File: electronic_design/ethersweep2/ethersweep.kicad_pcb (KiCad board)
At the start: 2 copper layers, 79 x 38 mm, 69 parts, among them J1 AVR-ISP-6, J2 Conn_01x02_Male, J3 Conn_01x04_Female, J4 Conn_01x02_Male, J5 Conn_01x02_Male, J6 HR911105A, J7 Conn_01x06_Female, J8 AVR-ISP-6, J9 Conn_01x06_Male, M1 Stepper_Motor_bipolar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

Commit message: small routing changes
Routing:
- net MISO: track 34.5 -> 36.3 mm
- net GND: vias 177 -> 192
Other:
- outline, holes or cut-outs redrawn

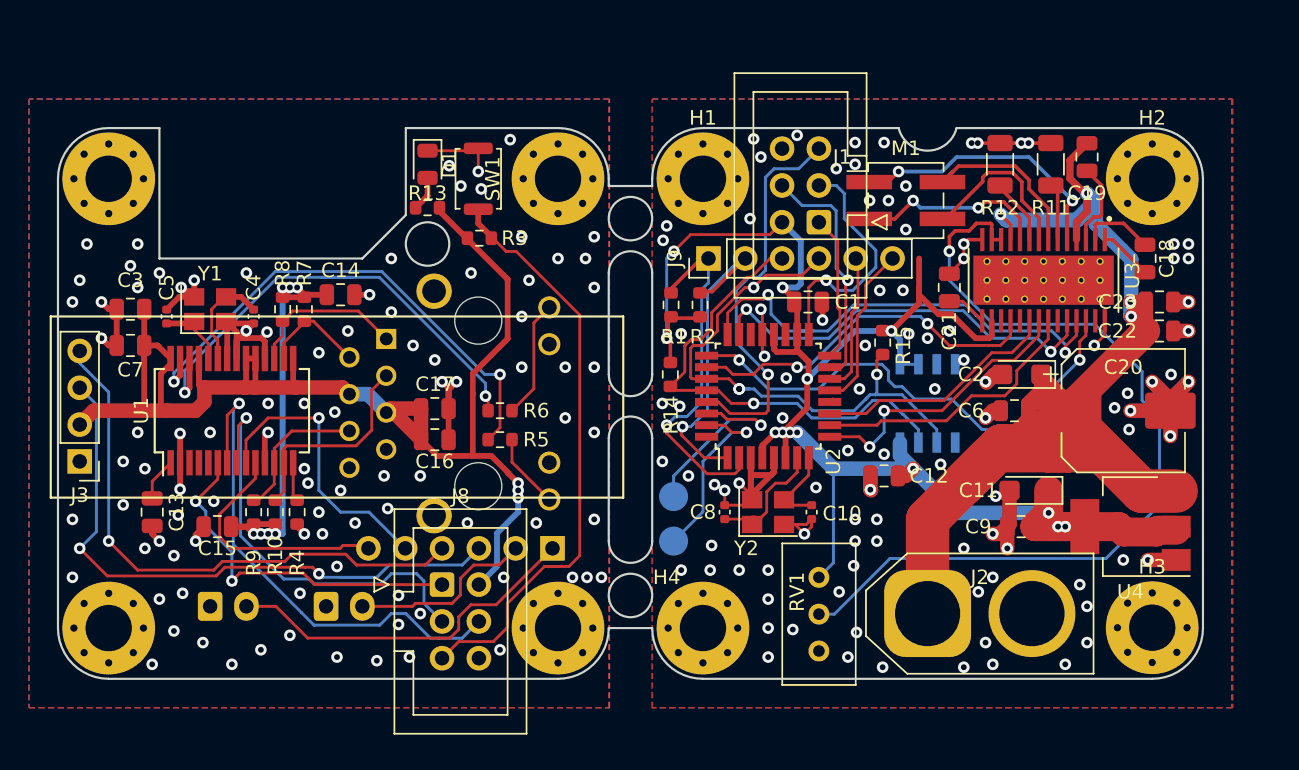
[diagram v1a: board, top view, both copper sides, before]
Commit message: added LCSC part numbers and changed some components for cheap manufacturing
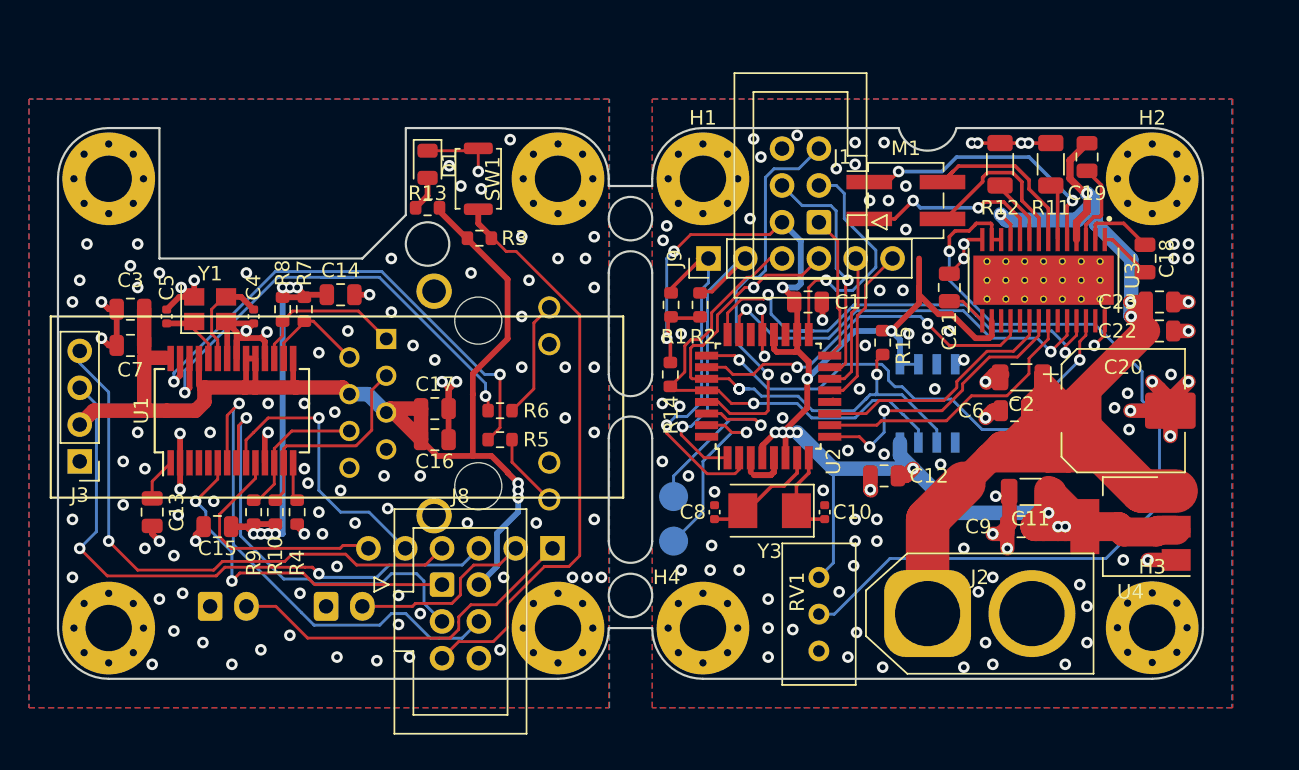
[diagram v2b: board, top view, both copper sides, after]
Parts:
- removed Y2: Crystal_8MHz, Crystal:Crystal_SMD_3225-4Pin_3.2x2.5mm
- added Y3: Crystal, Crystal:Crystal_SMD_5032-2Pin_5.0x3.2mm, F.Cu at (171.6, 107.4)
- C11, C2: value C22uF -> C4.7uF; footprint Capacitor_Tantalum_SMD:CP_EIA-3216-12_Kemet-S -> Capacitor_SMD:C_1206_3216Metric
- moved C10 0.90 mm to (175.4, 107.5), turned to 270 degrees
- moved C8 0.70 mm to (167.8, 107.5)
- moved C2 0.20 mm to (189.0, 98.2)
- moved C11 0.14 mm to (189.6, 106.1)
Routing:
- net GND: track 114.0 -> 92.9 mm, vias 192 -> 188
- net +3V3: track 226.6 -> 224.7 mm
- net +12V: track 116.7 -> 117.8 mm
- net Net-(C10-Pad2): track 5.66 -> 6.49 mm

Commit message: footprint changes, LCSC parts assigned, design changes
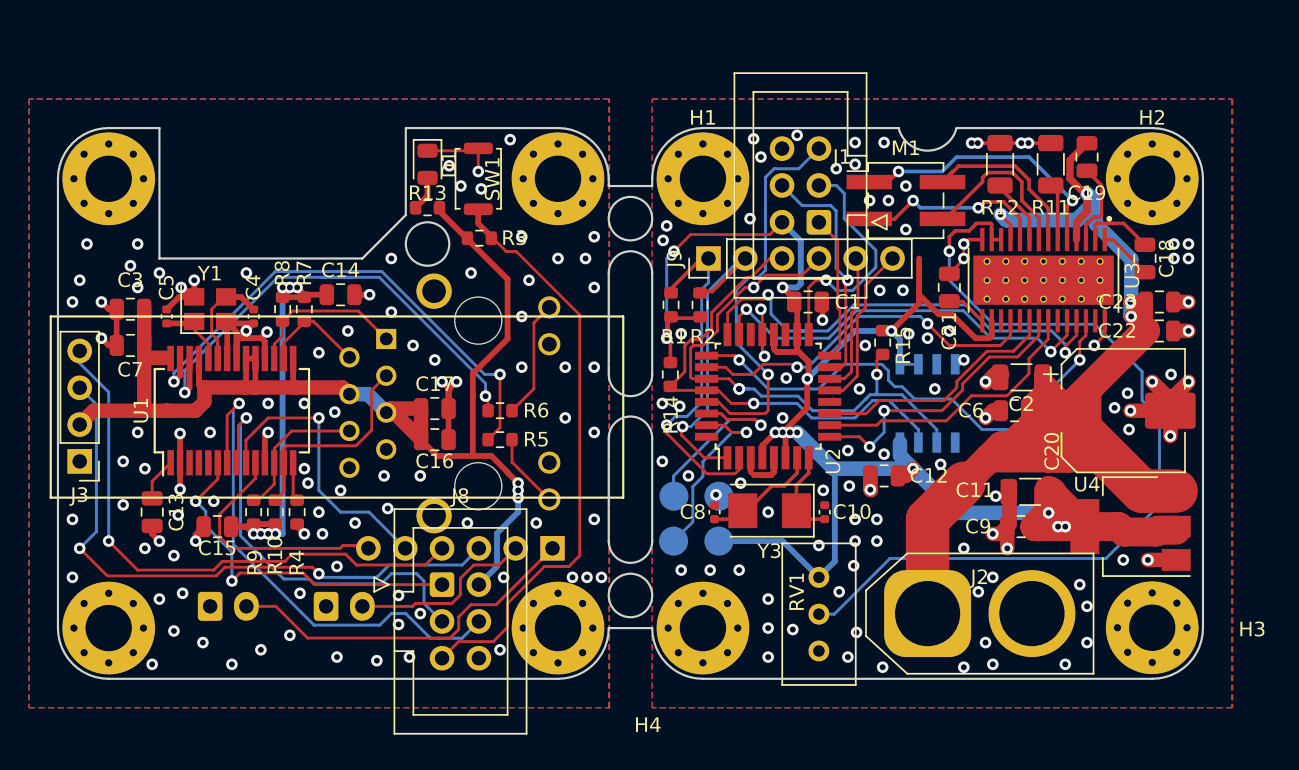
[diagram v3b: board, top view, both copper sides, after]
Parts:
- added TP1: TestPoint, TestPoint:TestPoint_Pad_D2.0mm, B.Cu at (168.1, 109.5)
- added TP2: TestPoint, TestPoint:TestPoint_Pad_D2.0mm, B.Cu at (168.1, 106.4)
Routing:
- net +3V3: track 224.7 -> 232.7 mm
- net GND: vias 188 -> 191
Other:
- board text added: "3.3V>"
- board text added: "GND>"
- board text added: "ethersweep"
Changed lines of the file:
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@@
   (general
     (thickness 1.6)
-    (drawings 47)
-    (tracks 1198)
+    (drawings 52)
+    (tracks 1206)
     (zones 0)
-    (modules 69)
+    (modules 71)
     (nets 62)
   )
@@
     (0 F.Cu signal)
     (31 B.Cu signal)
-    (32 B.Adhes user)
-    (33 F.Adhes user)
+    (32 B.Adhes user hide)
+    (33 F.Adhes user hide)
     (34 B.Paste user)
     (35 F.Paste user)
@@
   )
   (setup
-    (last_trace_width 2)
+    (last_trace_width 0.4)
     (user_trace_width 0.2)
     (user_trace_width 0.4)
@@
     (tags "mounting hole 3.2mm m3")
     (attr virtual)
-    (fp_text reference H4 (at -2.5 -3.5) (layer F.SilkS)
+    (fp_text reference H4 (at -3.8 6.7) (layer F.SilkS)
       (effects (font (size 1 1) (thickness 0.15)))
     )
@@
     (tags "mounting hole 3.2mm m3")
     (attr virtual)
-    (fp_text reference H3 (at 0 -4.2) (layer F.SilkS)
+    (fp_text reference H3 (at 6.9 0.124999) (layer F.SilkS)
       (effects (font (size 1 1) (thickness 0.15)))
     )
@@
     (tags "capacitor electrolytic")
     (attr smd)
-    (fp_text reference C20 (at 0 -3) (layer F.SilkS)
+    (fp_text reference C20 (at -4.9 2.8 90) (layer F.SilkS)
       (effects (font (size 1 1) (thickness 0.15)))
     )
@@
     (tags resistor)
     (attr smd)
-    (fp_text reference R9 (at -3.5 0 -90) (layer F.SilkS)
+    (fp_text reference R9 (at -3.5 0.1 90) (layer F.SilkS)
       (effects (font (size 1 1) (thickness 0.15)))
     )
@@
     (tags "CMS SOT")
     (attr smd)
-    (fp_text reference U4 (at 0 -4.5) (layer F.SilkS)
+    (fp_text reference U4 (at 3 2.9) (layer F.SilkS)
       (effects (font (size 1 1) (thickness 0.15)))
     )
@@
     (tags "mounting hole 3.2mm m3")
     (attr virtual)
-    (fp_text reference H7 (at 0 4.2) (layer B.SilkS)
+    (fp_text reference H7 (at -0.2 -6) (layer B.SilkS)
       (effects (font (size 1 1) (thickness 0.15)) (justify mirror))
     )
@@
     (tags "mounting hole 3.2mm m3")
     (attr virtual)
-    (fp_text reference H8 (at 0 4.2) (layer B.SilkS)
+    (fp_text reference H8 (at 0.2 -6.3) (layer B.SilkS)
       (effects (font (size 1 1) (thickness 0.15)) (justify mirror))
     )
@@
     (tags "test point SMD pad")
     (attr virtual)
-    (fp_text reference RX1 (at 0 1.998 270) (layer B.SilkS)
+    (fp_text reference RX1 (at -2 -0.074999) (layer B.SilkS)
       (effects (font (size 1 1) (thickness 0.15)) (justify mirror))
     )
@@
   )
   (module TestPoint:TestPoint_Pad_D2.0mm (layer B.Cu)
-    (at 164.974999 106.424999 90)
+    (at 165 106.4 90)
     (descr "SMD pad as test Point, diameter 2.0mm")
     (tags "test point SMD pad")
     (attr virtual)
-    (fp_text reference TX1 (at 0 1.998 270) (layer B.SilkS)
+    (fp_text reference TX1 (at 2 -0.1) (layer B.SilkS)
       (effects (font (size 1 1) (thickness 0.15)) (justify mirror))
     )
@@
     (descr "Through hole straight pin header, 1x06, 2.54mm pitch, single row")
     (tags "Through hole pin header THT 1x06 2.54mm single row")
-    (fp_text reference J7 (at 0 2.33 -90) (layer B.SilkS)
+    (fp_text reference J7 (at -17 2.88 -90) (layer B.SilkS)
       (effects (font (size 1 1) (thickness 0.15)) (justify mirror))
     )
@@
   )
   (module Capacitor_SMD:C_1206_3216Metric (layer F.Cu)
-    (at 189.6 106.1 180)
+    (at 189.575 106.1 180)
     (descr "Capacitor SMD 1206 (3216 Metric), square (rectangular) end terminal, IPC_7351 nominal, (Body size source: IPC-SM-782 page 76, https://www.pcb-3d.com/wordpress/wp-content/uploads/ipc-sm-782a_amendment_1_and_2.pdf), generated with kicad-footprint-generator")
     (tags capacitor)
     (attr smd)
-    (fp_text reference C11 (at 0 -1.85) (layer F.SilkS)
+    (fp_text reference C11 (at 3.8 0.1) (layer F.SilkS)
       (effects (font (size 1 1) (thickness 0.15)))
     )
@@
     )
   )
+  (module TestPoint:TestPoint_Pad_D2.0mm (layer B.Cu)
+    (at 168.1 109.5)
+    (descr "SMD pad as test Point, diameter 2.0mm")
+    (tags "test point SMD pad")
+    (attr virtual)
+    (fp_text reference TP1 (at -0.1 1.998) (layer B.SilkS)
+      (effects (font (size 1 1) (thickness 0.15)) (justify mirror))
+    )
+    (fp_text value TestPoint (at 0 -2.05) (layer B.Fab)
+      (effects (font (size 1 1) (thickness 0.15)) (justify mirror))
+    )
+    (fp_text user %R (at 0 2) (layer B.Fab)
+      (effects (font (size 1 1) (thickness 0.15)) (justify mirror))
+    )
+    (fp_circle (center 0 0) (end 1.5 0) (layer B.CrtYd) (width 0.05))
+    (fp_circle (center 0 0) (end 0 -1.2) (layer B.SilkS) (width 0.12))
+    (pad 1 smd circle (at 0 0) (size 2 2) (layers B.Cu B.Mask)
+      (net 14 +3V3))
+  )
+  (module TestPoint:TestPoint_Pad_D2.0mm (layer B.Cu)
+    (at 168.1 106.4)
+    (descr "SMD pad as test Point, diameter 2.0mm")
+    (tags "test point SMD pad")
+    (attr virtual)
+    (fp_text reference TP2 (at 0.2 -2) (layer B.SilkS)
+      (effects (font (size 1 1) (thickness 0.15)) (justify mirror))
+    )
+    (fp_text value TestPoint (at 0 -2.05) (layer B.Fab)
+      (effects (font (size 1 1) (thickness 0.15)) (justify mirror))
+    )
+    (fp_circle (center 0 0) (end 0 -1.2) (layer B.SilkS) (width 0.12))
+    (fp_circle (center 0 0) (end 1.5 0) (layer B.CrtYd) (width 0.05))
+    (fp_text user %R (at 0 2) (layer B.Fab)
+      (effects (font (size 1 1) (thickness 0.15)) (justify mirror))
+    )
+    (pad 1 smd circle (at 0 0) (size 2 2) (layers B.Cu B.Mask)
+      (net 1 GND))
+  )
+  (gr_poly (pts (xy 139.3 91) (xy 139.2 111) (xy 126.2 111) (xy 126.3 91)) (layer B.SilkS) (width 0.1))
+  (gr_text ethersweep (at 193.9 85.3) (layer B.SilkS)
+    (effects (font (size 2 2) (thickness 0.5)) (justify left mirror))
+  )
+  (gr_poly (pts (xy 178.7 103.1) (xy 165.4 103.1) (xy 165.4 93.1) (xy 178.7 93.1)) (layer B.SilkS) (width 0.1))
+  (gr_text 3.3V> (at 172.5 109.4) (layer B.SilkS)
+    (effects (font (size 1.5 1.5) (thickness 0.3)) (justify mirror))
+  )
+  (gr_text GND> (at 172.3 106.3) (layer B.SilkS)
+    (effects (font (size 1.5 1.5) (thickness 0.3)) (justify mirror))
+  )
   (gr_circle (center 167.5 104.25) (end 168.75 104.25) (layer F.Fab) (width 0.15))
   (gr_circle (center 167.5 104.25) (end 169.5 104.25) (layer F.Fab) (width 0.15))
@@
   (gr_arc (start 126 115.5) (end 126 119) (angle 90) (layer Edge.Cuts) (width 0.15))
   (gr_line (start 157 119) (end 126 119) (layer Edge.Cuts) (width 0.15))
+  (via (at 167.9 106.3) (size 0.8) (drill 0.4) (layers F.Cu B.Cu) (net 1))
   (segment (start 186.275 88.7) (end 185.3 88.7) (width 0.25) (layer F.Cu) (net 1))
   (segment (start 185.3 88.7) (end 185 89) (width 0.25) (layer F.Cu) (net 1))
@@
   (via (at 165.5 95.2) (size 0.8) (drill 0.4) (layers F.Cu B.Cu) (net 1))
   (via (at 164.2 104) (size 0.8) (drill 0.4) (layers F.Cu B.Cu) (net 1))
-  (via (at 167.6 109.8) (size 0.8) (drill 0.4) (layers F.Cu B.Cu) (net 1))
-  (via (at 167.8 106.1) (size 0.8) (drill 0.4) (layers F.Cu B.Cu) (net 1))
   (via (at 179.2 92.2) (size 0.8) (drill 0.4) (layers F.Cu B.Cu) (net 1))
   (via (at 180.8 92.2) (size 0.8) (drill 0.4) (layers F.Cu B.Cu) (net 1))
@@
   (via (at 199.3 98) (size 0.8) (drill 0.4) (layers F.Cu B.Cu) (net 1))
   (via (at 175.3 106) (size 0.8) (drill 0.4) (layers F.Cu B.Cu) (net 1))
+  (via (at 177.1 105.7) (size 0.8) (drill 0.4) (layers F.Cu B.Cu) (net 1))
+  (via (at 175 109.8) (size 0.8) (drill 0.4) (layers F.Cu B.Cu) (net 1))
+  (via (at 171.5 107.5) (size 0.8) (drill 0.4) (layers F.Cu B.Cu) (net 1))
+  (via (at 169.6 105.5) (size 0.8) (drill 0.4) (layers F.Cu B.Cu) (net 1))
   (segment (start 148 85.675) (end 147.175 86.5) (width 0.4) (layer F.Cu) (net 2))
   (segment (start 148 84.4375) (end 148 85.675) (width 0.4) (layer F.Cu) (net 2))
@@
   (segment (start 181.865 97.3) (end 180.595 97.3) (width 0.2) (layer B.Cu) (net 14))
   (segment (start 172.46 87.5) (end 172.46 87.66712) (width 0.4) (layer F.Cu) (net 14))
-  (segment (start 176 111) (end 175 112) (width 0.2) (layer B.Cu) (net 14))
-  (segment (start 176 104.5) (end 176 111) (width 0.2) (layer B.Cu) (net 14))
   (segment (start 184.55 107.55) (end 190.85 107.55) (width 1) (layer B.Cu) (net 14))
   (segment (start 181.5 104.5) (end 184.55 107.55) (width 1) (layer B.Cu) (net 14))
@@
   (segment (start 191.075 106.225) (end 193.35 108.5) (width 2) (layer F.Cu) (net 14))
   (segment (start 191.075 106.1) (end 191.075 106.225) (width 2) (layer F.Cu) (net 14))
+  (segment (start 172.5 109.5) (end 175 112) (width 0.4) (layer B.Cu) (net 14))
+  (segment (start 168.1 109.5) (end 172.5 109.5) (width 0.4) (layer B.Cu) (net 14))
+  (segment (start 176.100001 104.600001) (end 176 104.5) (width 0.4) (layer B.Cu) (net 14))
+  (segment (start 176.100001 110.899999) (end 176.100001 104.600001) (width 0.4) (layer B.Cu) (net 14))
+  (segment (start 175 112) (end 176.100001 110.899999) (width 0.4) (layer B.Cu) (net 14))
   (segment (start 137.5 109) (end 137.5 109) (width 0.4) (layer F.Cu) (net 15))
   (via (at 137.5 109) (size 0.8) (drill 0.4) (layers F.Cu B.Cu) (net 15))
@@
   (segment (start 170 102) (end 169 102) (width 0.2) (layer B.Cu) (net 22))
   (segment (start 169 102) (end 167 104) (width 0.2) (layer B.Cu) (net 22))
-  (segment (start 167 107.474999) (end 164.974999 109.5) (width 0.2) (layer B.Cu) (net 22))
-  (segment (start 167 104) (end 167 107.474999) (width 0.2) (layer B.Cu) (net 22))
+  (segment (start 166.300001 108.174998) (end 164.974999 109.5) (width 0.2) (layer B.Cu) (net 22))
+  (segment (start 167 105.036002) (end 166.300001 105.736001) (width 0.2) (layer B.Cu) (net 22))
+  (segment (start 166.300001 105.736001) (end 166.300001 108.174998) (width 0.2) (layer B.Cu) (net 22))
+  (segment (start 167 104) (end 167 105.036002) (width 0.2) (layer B.Cu) (net 22))
   (segment (start 168.25 100.7) (end 168.525 100.975) (width 0.2) (layer F.Cu) (net 23))
   (segment (start 170.600011 101.100011) (end 171 101.5) (width 0.2) (layer F.Cu) (net 23))
